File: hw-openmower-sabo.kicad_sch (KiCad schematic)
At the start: 26 parts, among them J1 Conn_01x05_Pin, J19 Conn_01x02, J20 Conn_01x02, J31 Conn_01x03_Pin, J32 Conn_02x08_Odd_Even, J33 Molex 470531000, M1 Fan, M2 Fan, Q4 AO3400A, Q5 AO3400A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

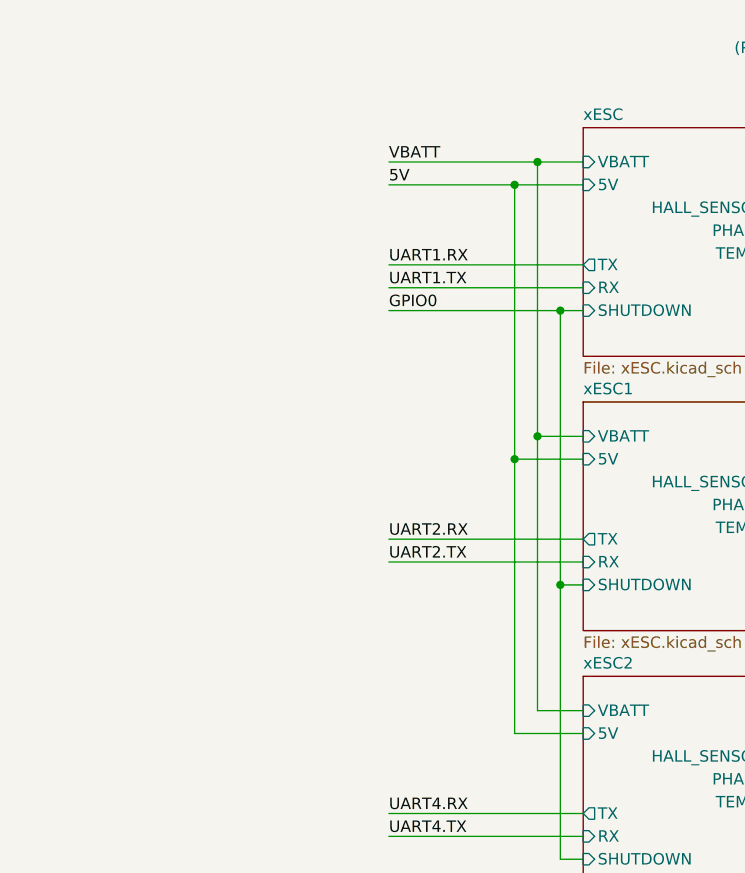
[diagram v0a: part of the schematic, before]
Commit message: KiCAD 10.x, Mow-ESC-Fuse, Improve power traces
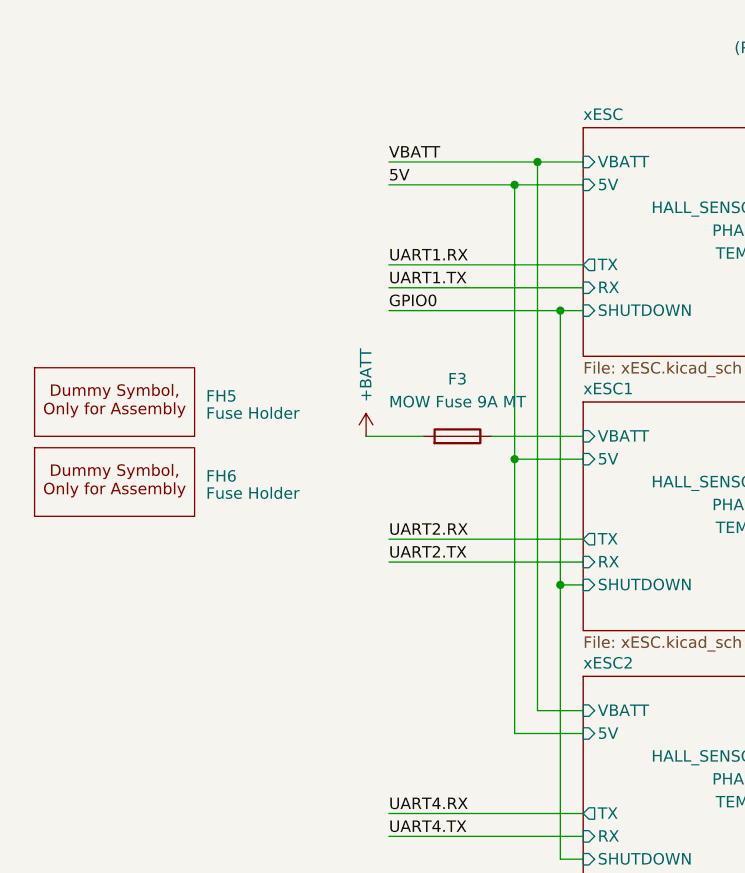
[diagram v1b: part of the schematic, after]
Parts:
- added F3: MOW Fuse 9A MT, local_Connectors:Fuseholder_Clip-5x20mm_XFCN_XF-003_Inline_P20.00x5.00mm_Horizontal, symbol Device:Fuse
- added FH5, FH6: Fuse Holder, xtech:Dummy, symbol xtech:Dummy
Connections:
- new net +BATT: F3.2
- new net xESC1/VBATT: F3.1

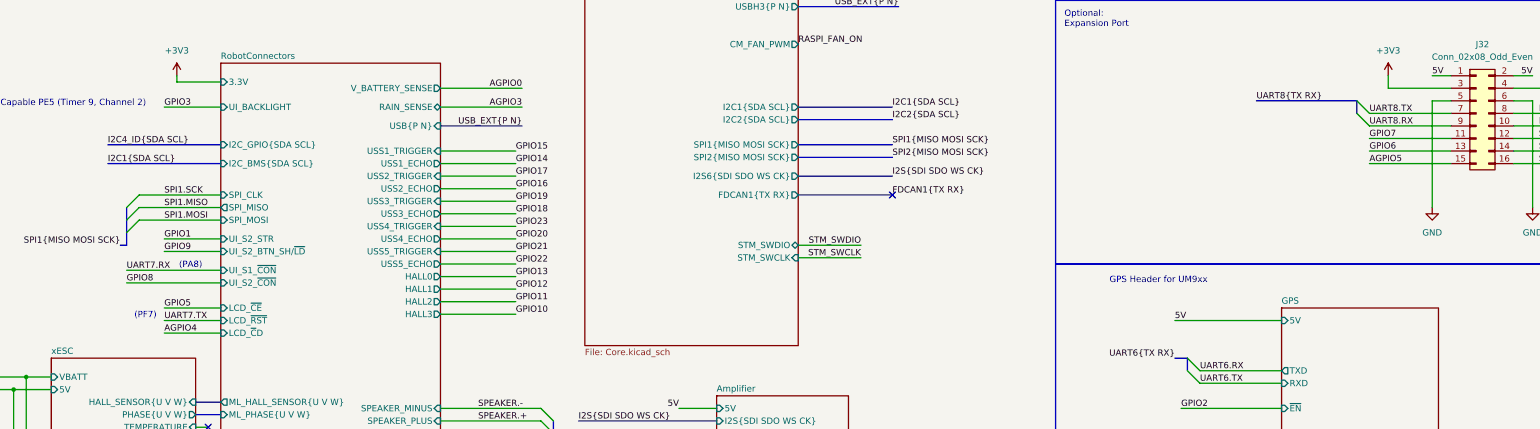
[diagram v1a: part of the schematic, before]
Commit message: Free UART7 for alternative BMS usage
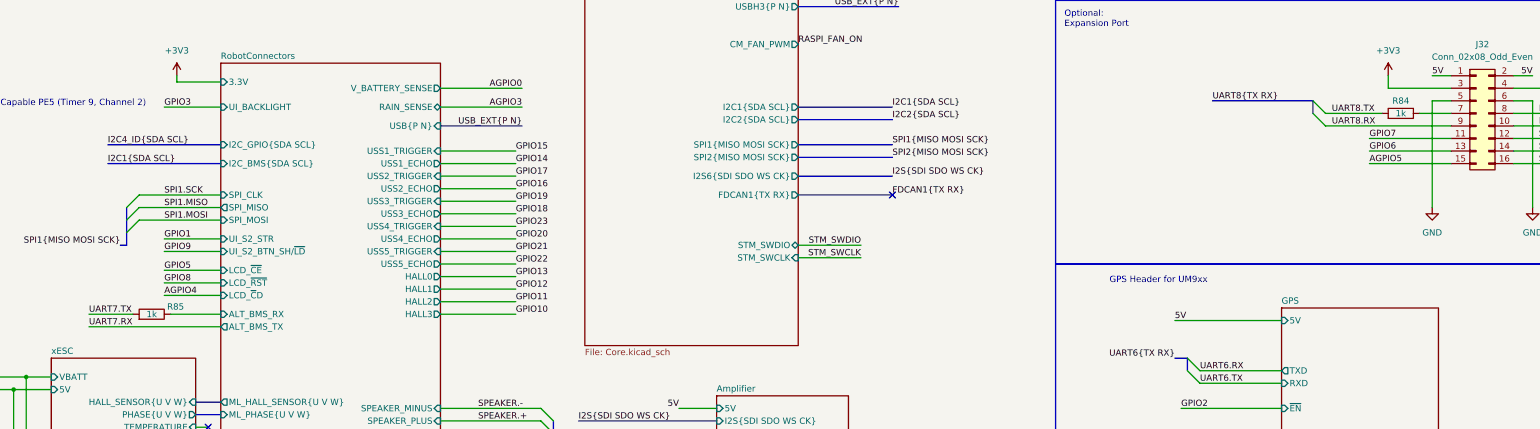
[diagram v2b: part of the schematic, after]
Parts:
- added R84, R85: 1k, Resistor_SMD:R_0402_1005Metric, symbol Device:R
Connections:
- net UART7.TX: now also R85.2
- net UART8.TX: now also R84.2; no longer J32.7 (Pin_7)
- new net: J32.7 (Pin_7), R84.1
- new net RobotConnectors/ALT_BMS_RX: R85.1
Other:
- sheet RobotConnectors ports: added ALT_BMS_RX, ALT_BMS_TX; removed UI_S1_~{CON}, UI_S2_~{CON}
- note removed: "(PA8)"
- note removed: "(PF7)"

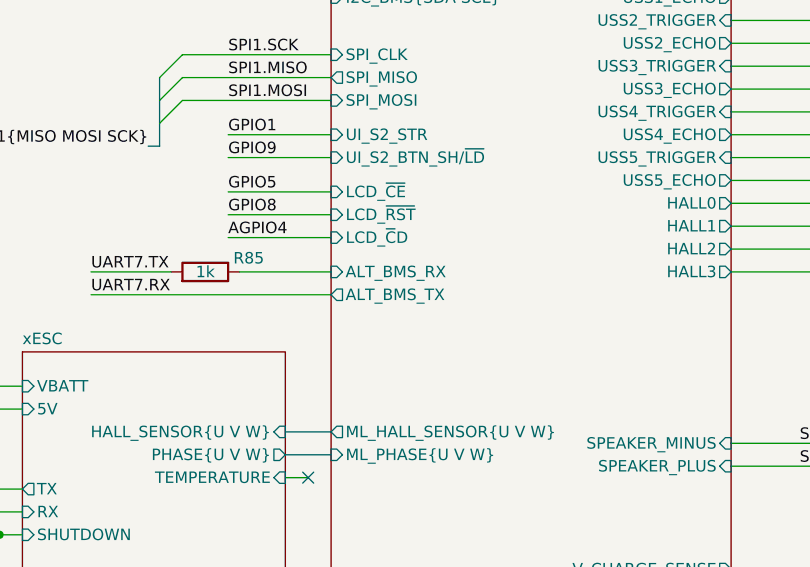
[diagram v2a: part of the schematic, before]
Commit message: Optional 6-9A charge current via Fsw 200kHz solder jumper
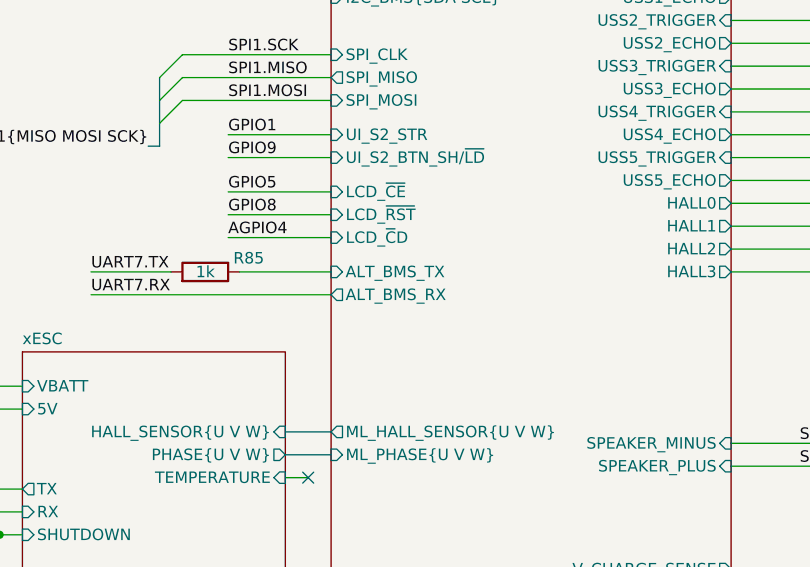
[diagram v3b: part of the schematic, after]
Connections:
- net RobotConnectors/ALT_BMS_RX renamed RobotConnectors/ALT_BMS_TX
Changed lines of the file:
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@@
 			)
 		)
-		(pin "ALT_BMS_RX" input
+		(pin "ALT_BMS_TX" input
 			(at 72.39 177.8 180)
 			(effects
@@
 			)
 		)
-		(pin "ALT_BMS_TX" output
+		(pin "ALT_BMS_RX" output
 			(at 72.39 180.34 180)
 			(effects

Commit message: Production state
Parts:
- F3: now not fitted
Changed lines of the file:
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@@
 	(title_block
 		(title "OpenMower SABO Carrierboard for Series I & II")
-		(date "2026-04-10")
-		(rev "v0.5-dev")
+		(date "2026-05-26")
+		(rev "v0.5")
 		(company "Apeheanger <joerg@ebeling.ws> for OpenMower")
 		(comment 1 "This design is licensed under CC BY-NC 4.0")
@@
 		(on_board yes)
 		(in_pos_files yes)
-		(dnp no)
+		(dnp yes)
 		(property "Reference" "F3"
 			(at 24.13 214.63 90)
